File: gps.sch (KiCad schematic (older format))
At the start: 80 parts

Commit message: removed unncesary ICs for clock source part
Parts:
- removed C16: 0u1, 0402, symbol CAP
- removed C17, C27, C33, C40: 0u1/RF, 0603, symbol CAP
- removed C18, C24, C28: 0u1, 0603, symbol CAP
- removed C25, C38: 0u1/RF, 0402, symbol CAP
- removed C29, C42: 10u/RF, 0805, symbol CAPP
- removed C30: 10u, 0805, symbol CAPP
- removed DA7, DA8, DA9: AD8063, SOIC-8, symbol IC_AD8063
- removed R1: 51, 0402, symbol RES
- removed R10, R12, R2, R3, R4, R5, R6, R7: 20k, 0603, symbol RES
- removed R11: 20k, symbol RES
- removed R61, R62, R63: RES, 0402, symbol RES
- removed R8, R9: 0, 0603, symbol RES
- removed XP2: 16MHz_IN, symbol COAX_CONNECTOR
- removed XP3: 16MHz_OUT, symbol COAX_CONNECTOR
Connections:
- net labels removed: ~TCXO_dsbl, ~ext_freq_dsbl
- wire segments 262 -> 128
- no-connect marks 7 -> 1
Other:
- note removed: "Ref Freq"
- moved on the sheet: C1, C10, C11, C12, C15, C19, C2, C20, C21, C26, C3, C31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

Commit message: removed power supply - this will likelly come from fpga main board
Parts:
- removed C10, C11, C12: 0u01, 0603, symbol CAP
- removed C19, C20, C21: 2u2, 0603, symbol CAP
- removed C2: 10u, 0805, symbol CAPP
- removed C5, C6, C7: 0u1, 0603, symbol CAP
- removed DA2, DA3, DA4: TPS79230, SOT23, symbol IC_TPS79230
- removed VD1: 1A, D0214AC, symbol DIODE
- removed XP1: CONN_02_M, symbol CONN_02_M
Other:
- note removed: "Power Supply"
- moved on the sheet: C1, C15, C26, C3, C31, C32, C34, C36, C37, C39, C4, C41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

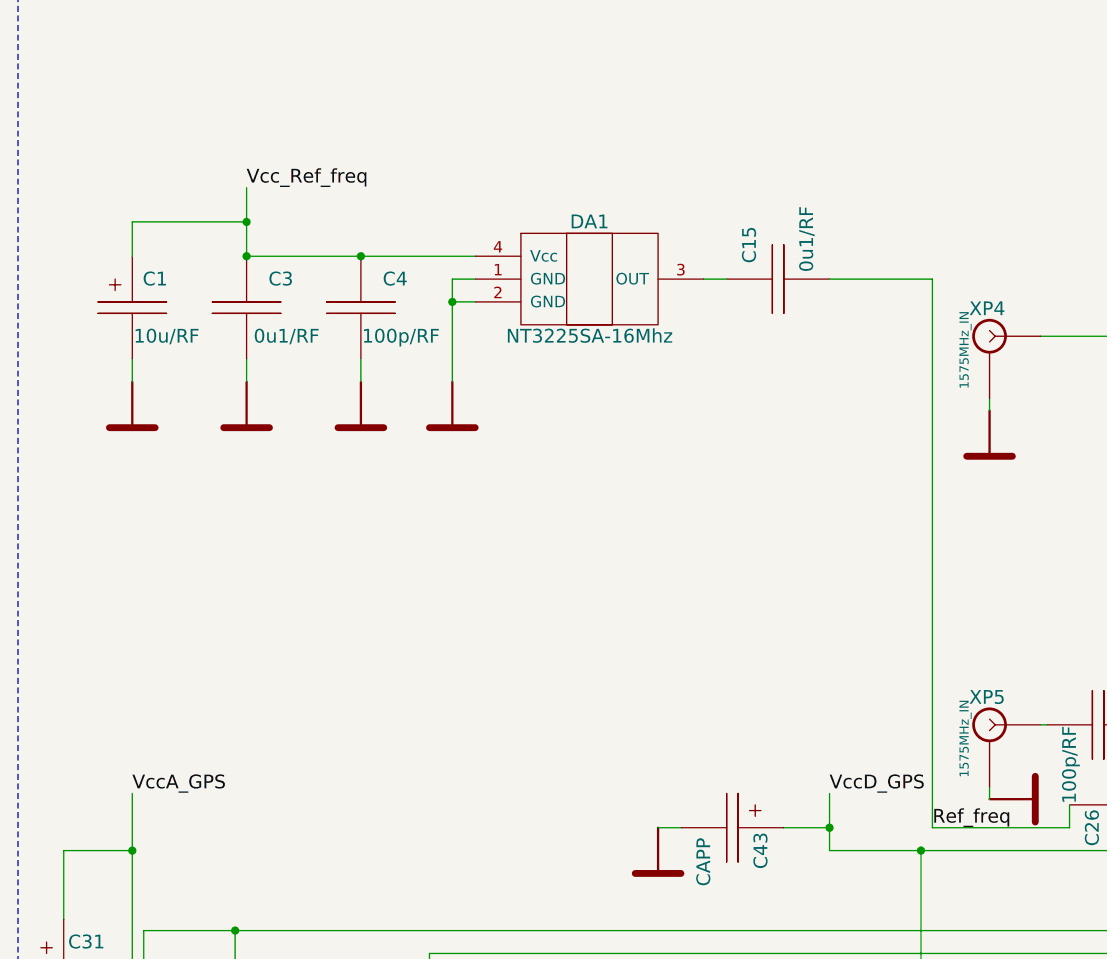
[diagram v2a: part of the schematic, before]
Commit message: Vcc renaming
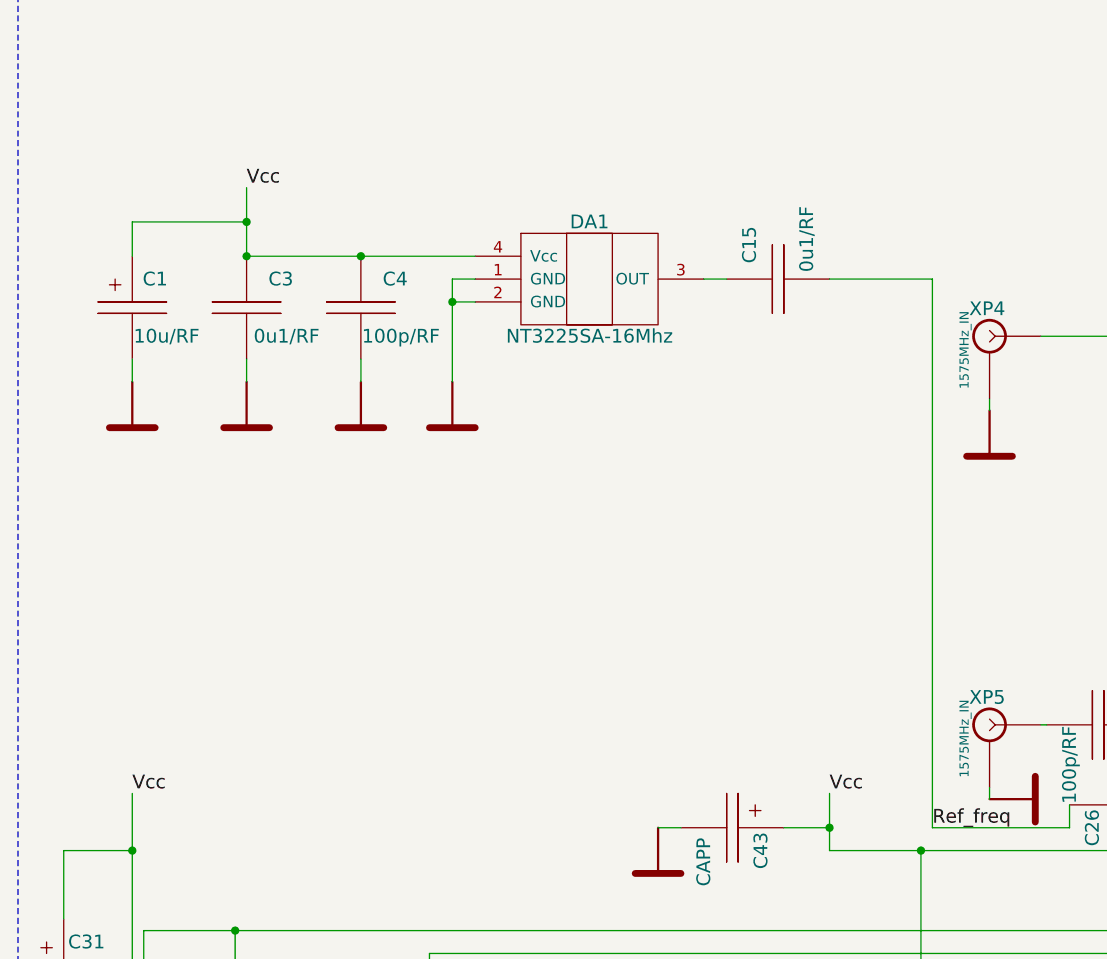
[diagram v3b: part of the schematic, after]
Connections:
- net VccD_GPS is gone; now on net Vcc: C43.1, C45.1, C46.1, C47.1, C50.1, DA10.14 (VccD), DA10.19 (VccADC), DA10.7 (~SHDN)
- net Vcc_Ref_freq is gone; now on net Vcc: C1.1, C3.1, C4.1, DA1.4 (Vcc)
- net VccA_GPS renamed Vcc
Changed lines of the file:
@@
-EESchema Schematic File Version 2  date Sun 16 Sep 2012 11:19:59 AM COT
+EESchema Schematic File Version 2  date Sun 16 Sep 2012 11:22:33 AM COT
 LIBS:lib_passive
 LIBS:lib_active
@@
 $EndComp
 Text Label 12500 11700 0    60   ~ 0
-VccA_GPS
+Vcc
 $Comp
 L POWER_GND #07
@@
 GPS-Receiver
 Text Label 15550 11700 0    60   ~ 0
-VccD_GPS
+Vcc
 Text Label 18900 11700 0    60   ~ 0
 I1
@@
 Ref_freq
 Text Label 13000 9050 0    60   ~ 0
-Vcc_Ref_freq
+Vcc
 Text Label 17200 11900 0    60   ~ 0
 ~CS

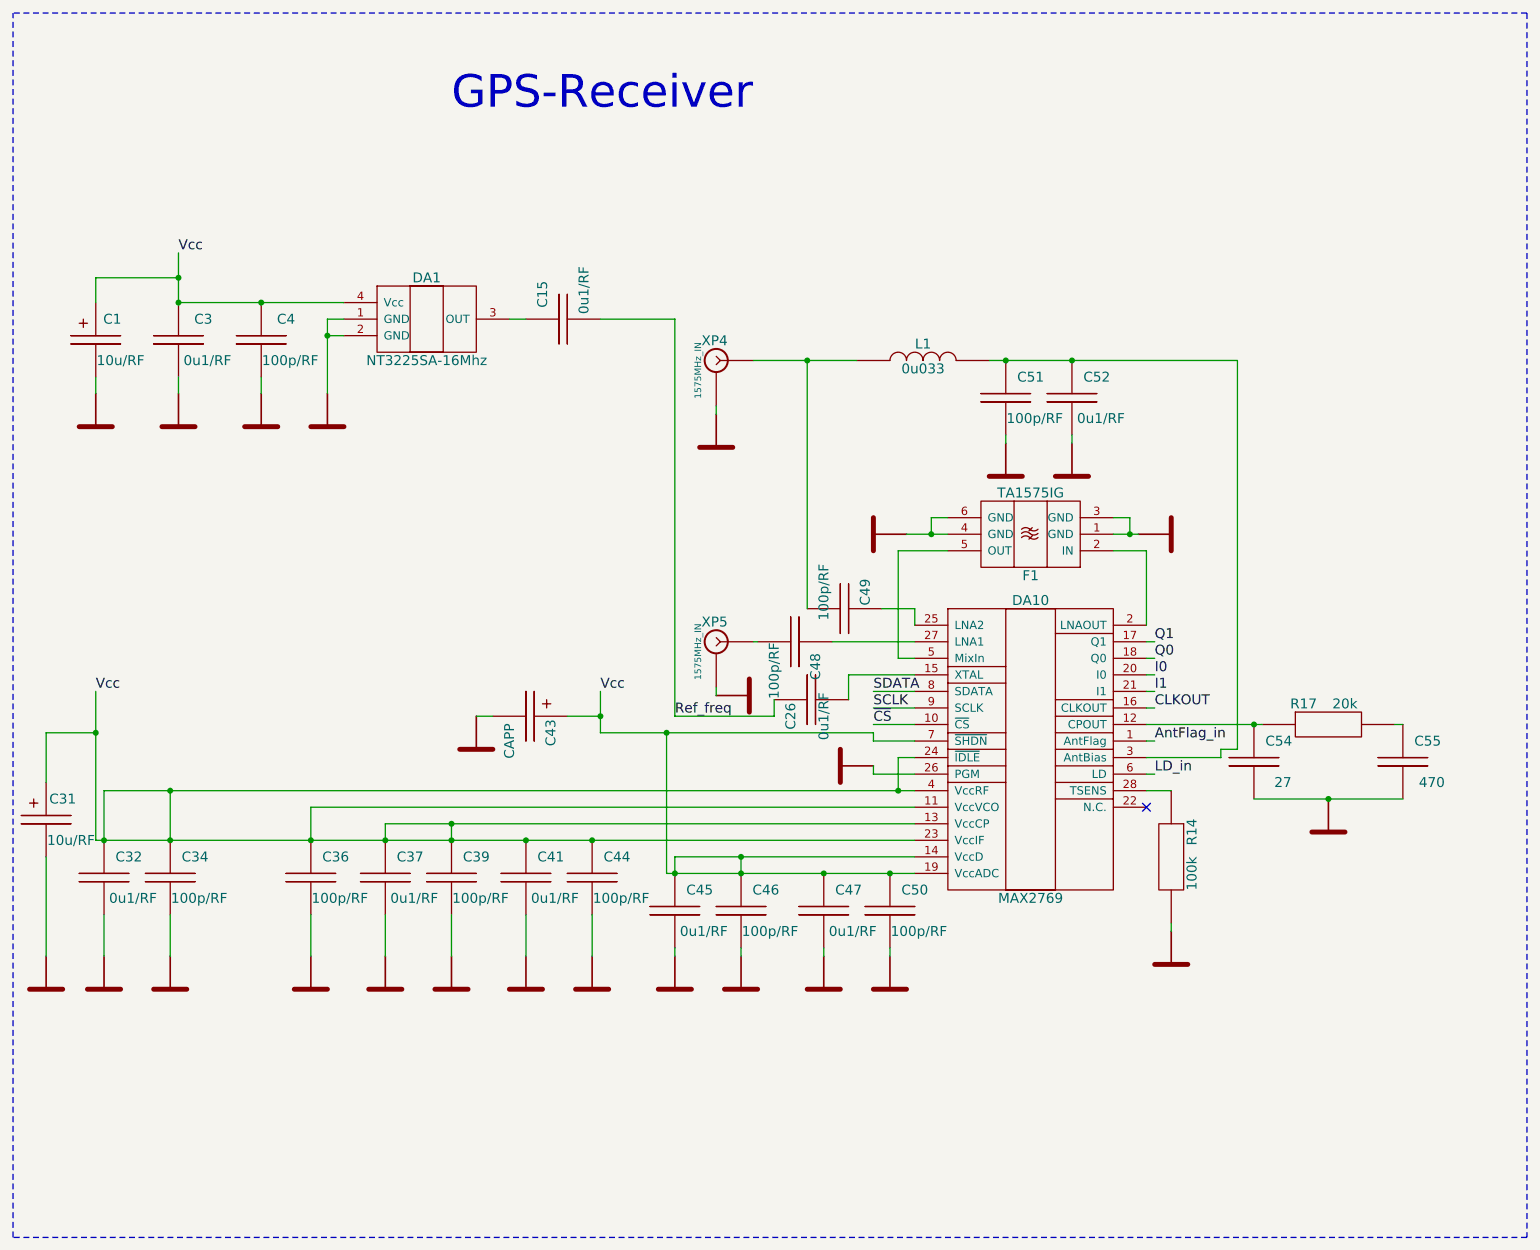
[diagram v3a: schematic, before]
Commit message: small CRC fix
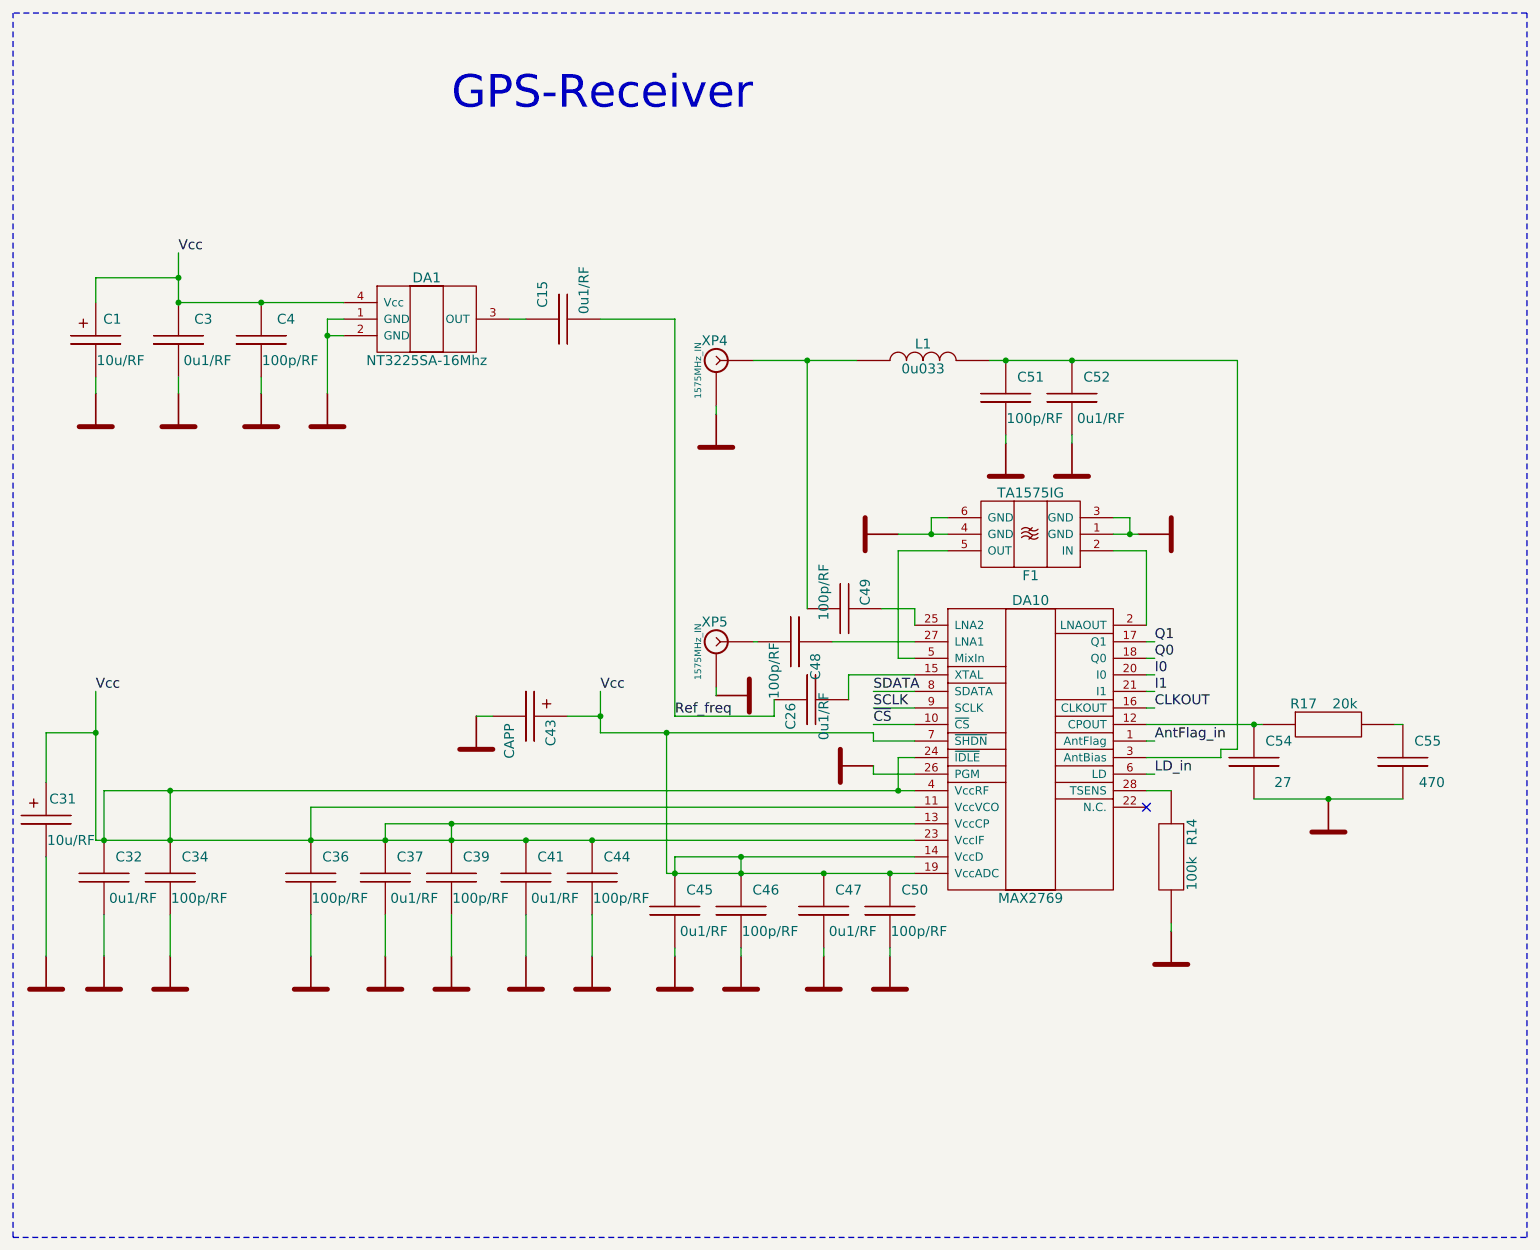
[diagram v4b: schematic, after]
